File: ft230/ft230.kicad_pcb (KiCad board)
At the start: 2 copper layers, 17 x 10.2 mm, 14 parts, among them J1 USB_OTG, J2 Conn_01x04, U1 FT230XQ

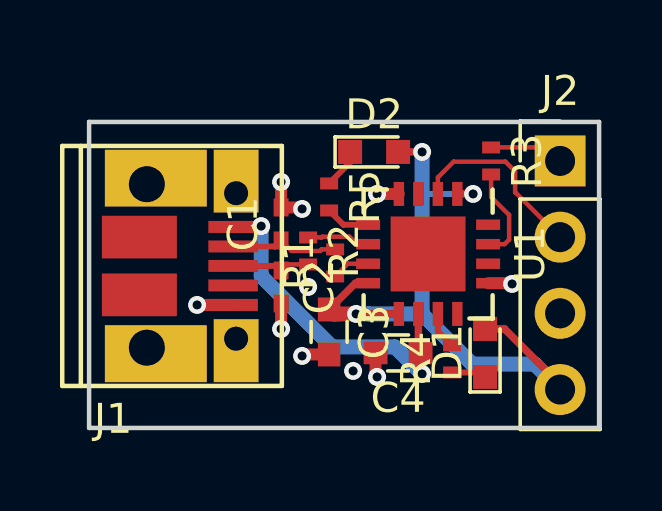
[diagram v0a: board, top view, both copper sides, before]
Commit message: exchange Rx and Tx
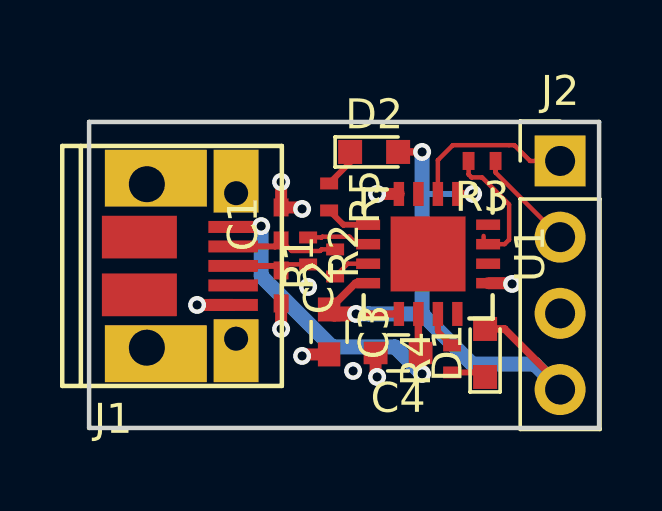
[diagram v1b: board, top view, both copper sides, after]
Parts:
- moved R3 0.30 mm to (153.1, 71.3), turned to 180 degrees
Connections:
- J1 pad 4: Net-(J1-Pad4) -> (no net)
- J2 pad 1: Net-(J2-Pad1) -> /Rx
- J2 pad 2: Net-(J2-Pad2) -> /Tx
- R3 pad 1: Net-(J2-Pad1) -> /Tx
- U1 pad 12: Net-(U1-Pad12) -> (no net)
- U1 pad 14: Net-(U1-Pad14) -> (no net)
- U1 pad 16: Net-(U1-Pad16) -> (no net)
- U1 pad 2: Net-(J2-Pad2) -> /Rx
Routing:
- net Net-(J2-Pad2): track 6.29 -> 0.00 mm
- net /Rx: track 0.00 -> 6.26 mm
- net /Tx: track 0.00 -> 3.43 mm
- net Net-(J2-Pad1): track 2.49 -> 0.00 mm
- net Net-(R3-Pad2): track 3.19 -> 4.25 mm
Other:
- board text added: "3.3V"

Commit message: update
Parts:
- added R6: 120, Resistors_SMD:R_0402_NoSilk, F.Cu at (151.8, 71.0)
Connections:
- J1 pad 4: (no net) -> Net-(J1-Pad4)
- U1 pad 12: (no net) -> Net-(U1-Pad12)
- U1 pad 14: (no net) -> Net-(U1-Pad14)
- U1 pad 16: (no net) -> Net-(U1-Pad16)
- U1 pad 2: /Rx -> Net-(R6-Pad2)
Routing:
- net /Rx: track 6.26 -> 4.85 mm
- net Net-(R6-Pad2): track 0.00 -> 1.02 mm
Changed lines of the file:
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@@
-(kicad_pcb (version 20170922) (host pcbnew no-vcs-found-0b1eb56~60~ubuntu17.04.1)
+(kicad_pcb (version 20170922) (host pcbnew no-vcs-found-fc5e8e5~60~ubuntu17.04.1)
 (general
   (thickness 1.6)
   (drawings 21)
-  (tracks 99)
+  (tracks 97)
   (zones 0)
-  (modules 14)
-  (nets 15)
+  (modules 15)
+  (nets 20)
 )
 (page A4)
@@
 (net 13 /Rx)
 (net 14 /Tx)
+(net 15 "Net-(J1-Pad4)")
+(net 16 "Net-(R6-Pad2)")
+(net 17 "Net-(U1-Pad12)")
+(net 18 "Net-(U1-Pad14)")
+(net 19 "Net-(U1-Pad16)")
 (net_class Default "This is the default net class."
   (clearance 0.15)
@@
   (add_net "Net-(D1-Pad1)")
   (add_net "Net-(D2-Pad1)")
+  (add_net "Net-(J1-Pad4)")
   (add_net "Net-(R1-Pad1)")
   (add_net "Net-(R2-Pad1)")
@@
   (add_net "Net-(R4-Pad2)")
   (add_net "Net-(R5-Pad2)")
+  (add_net "Net-(R6-Pad2)")
+  (add_net "Net-(U1-Pad12)")
+  (add_net "Net-(U1-Pad14)")
+  (add_net "Net-(U1-Pad16)")
 )
   (module Capacitors_SMD:C_0402_NoSilk (layer F.Cu)
@@
     (pad 3 smd rect (at -2 0.0009) (size 1.65 0.4) (layers F.Cu F.Paste F.Mask)
       (net 3 "Net-(C2-Pad1)"))
-    (pad 4 smd rect (at -2 -0.65) (size 1.65 0.4) (layers F.Cu F.Paste F.Mask))
+    (pad 4 smd rect (at -2 -0.65) (size 1.65 0.4) (layers F.Cu F.Paste F.Mask)
+      (net 15 "Net-(J1-Pad4)"))
     (pad 5 smd rect (at -2 -1.3) (size 1.65 0.4) (layers F.Cu F.Paste F.Mask)
       (net 1 GND))
@@
       (net 4 +3V3))
     (pad 2 smd rect (at -2 -0.325 270) (size 0.8 0.35) (layers F.Cu F.Paste F.Mask)
-      (net 13 /Rx))
+      (net 16 "Net-(R6-Pad2)"))
     (pad 3 smd rect (at -2 0.325 270) (size 0.8 0.35) (layers F.Cu F.Paste F.Mask)
       (net 1 GND))
@@
     (pad 11 smd rect (at 2 -0.325 270) (size 0.8 0.35) (layers F.Cu F.Paste F.Mask)
       (net 11 "Net-(R4-Pad2)"))
-    (pad 12 smd rect (at 2 -0.975 270) (size 0.8 0.35) (layers F.Cu F.Paste F.Mask))
+    (pad 12 smd rect (at 2 -0.975 270) (size 0.8 0.35) (layers F.Cu F.Paste F.Mask)
+      (net 17 "Net-(U1-Pad12)"))
     (pad 13 smd rect (at 0.975 -2) (size 0.8 0.35) (layers F.Cu F.Paste F.Mask)
       (net 1 GND))
-    (pad 14 smd rect (at 0.325 -2) (size 0.8 0.35) (layers F.Cu F.Paste F.Mask))
+    (pad 14 smd rect (at 0.325 -2) (size 0.8 0.35) (layers F.Cu F.Paste F.Mask)
+      (net 18 "Net-(U1-Pad14)"))
     (pad 15 smd rect (at -0.325 -2) (size 0.8 0.35) (layers F.Cu F.Paste F.Mask)
       (net 10 "Net-(R3-Pad2)"))
-    (pad 16 smd rect (at -0.975 -2) (size 0.8 0.35) (layers F.Cu F.Paste F.Mask))
+    (pad 16 smd rect (at -0.975 -2) (size 0.8 0.35) (layers F.Cu F.Paste F.Mask)
+      (net 19 "Net-(U1-Pad16)"))
     (pad 17 smd rect (at 0.625 0.625 270) (size 1.25 1.25) (layers F.Cu F.Paste F.Mask)
       (net 1 GND) (solder_paste_margin_ratio -0.2))
@@
       (net 1 GND) (solder_paste_margin_ratio -0.2))
     (model ${KISYS3DMOD}/Housings_DFN_QFN.3dshapes/QFN-16-1EP_4x4mm_Pitch0.65mm.wrl
+      (at (xyz 0 0 0))
+      (scale (xyz 1 1 1))
+      (rotate (xyz 0 0 0))
+    )
+  )
+  (module Resistors_SMD:R_0402_NoSilk (layer F.Cu)
+    (at 151.8 71 270)
+    (descr "Resistor SMD 0402, reflow soldering, Vishay (see dcrcw.pdf)")
+    (tags "resistor 0402")
+    (attr smd)
+    (fp_text reference R6 (at 0 -1.2 270) (layer F.SilkS)
+      (effects (font (size 1 1) (thickness 0.15)))
+    )
+    (fp_text value 120 (at 0 1.25 270) (layer F.Fab)
+      (effects (font (size 1 1) (thickness 0.15)))
+    )
+    (fp_text user %R (at 0 -1.2 270) (layer F.Fab)
+      (effects (font (size 1 1) (thickness 0.15)))
+    )
+    (fp_line (start -0.5 0.25) (end -0.5 -0.25) (layer F.Fab) (width 0.1))
+    (fp_line (start 0.5 0.25) (end -0.5 0.25) (layer F.Fab) (width 0.1))
+    (fp_line (start 0.5 -0.25) (end 0.5 0.25) (layer F.Fab) (width 0.1))
+    (fp_line (start -0.5 -0.25) (end 0.5 -0.25) (layer F.Fab) (width 0.1))
+    (fp_line (start -0.8 -0.45) (end 0.8 -0.45) (layer F.CrtYd) (width 0.05))
+    (fp_line (start -0.8 -0.45) (end -0.8 0.45) (layer F.CrtYd) (width 0.05))
+    (fp_line (start 0.8 0.45) (end 0.8 -0.45) (layer F.CrtYd) (width 0.05))
+    (fp_line (start 0.8 0.45) (end -0.8 0.45) (layer F.CrtYd) (width 0.05))
+    (pad 1 smd rect (at -0.45 0 270) (size 0.4 0.6) (layers F.Cu F.Paste F.Mask)
+      (net 13 /Rx))
+    (pad 2 smd rect (at 0.45 0 270) (size 0.4 0.6) (layers F.Cu F.Paste F.Mask)
+      (net 16 "Net-(R6-Pad2)"))
+    (model ${KISYS3DMOD}/Resistors_SMD.3dshapes/R_0402.wrl
       (at (xyz 0 0 0))
       (scale (xyz 1 1 1))
@@
   (segment (start 154 73.925) (end 153.85 74.075) (width 0.15) (layer F.Cu) (net 10))
   (segment (start 153.1 71.85) (end 154 72.75) (width 0.15) (layer F.Cu) (net 10))
-  (segment (start 153.15 73.8) (end 153.15 73.9) (width 0.15) (layer F.Cu) (net 10))
-  (segment (start 152.125001 70.774999) (end 154 70.774999) (width 0.15) (layer F.Cu) (net 13))
-  (segment (start 155.7 71.3) (end 154.7 71.3) (width 0.15) (layer F.Cu) (net 13))
-  (segment (start 154.7 71.3) (end 154.174999 70.774999) (width 0.15) (layer F.Cu) (net 13))
-  (segment (start 154.174999 70.774999) (end 154 70.774999) (width 0.15) (layer F.Cu) (net 13))
-  (segment (start 151.625 71.275) (end 152.125001 70.774999) (width 0.15) (layer F.Cu) (net 13))
-  (segment (start 151.625 72.4) (end 151.625 71.275) (width 0.15) (layer F.Cu) (net 13))
+  (segment (start 151.8 70.55) (end 153.95 70.55) (width 0.15) (layer F.Cu) (net 13))
+  (segment (start 153.95 70.55) (end 154.7 71.3) (width 0.15) (layer F.Cu) (net 13))
+  (segment (start 154.7 71.3) (end 155.7 71.3) (width 0.15) (layer F.Cu) (net 13))
   (segment (start 155.25 70.85) (end 155.7 71.3) (width 0.15) (layer F.Cu) (net 13))
   (segment (start 149.3 74.725) (end 148.625 74.725) (width 0.15) (layer F.Cu) (net 8))
@@
   (segment (start 155.7 73.84) (end 153.55 71.69) (width 0.15) (layer F.Cu) (net 14))
   (segment (start 153.55 71.69) (end 153.55 71.6) (width 0.15) (layer F.Cu) (net 14))
+  (segment (start 151.625 72.4) (end 151.625 71.625) (width 0.2) (layer F.Cu) (net 16))
+  (segment (start 151.625 71.625) (end 151.8 71.45) (width 0.2) (layer F.Cu) (net 16))
   (zone (net 1) (net_name GND) (layer F.Cu) (hatch edge 0.508)
     (connect_pads yes (clearance 0.15))
